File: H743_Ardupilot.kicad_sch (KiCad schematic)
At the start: 8 parts, among them U1 USBLC6-2P6

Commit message: upsadte SPI4 set to Baro
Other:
- sheet ANALOG_SENS ports: added ADC_AIRSPEED, ADC_VBAT1, ADC_VBAT2; removed none
- sheet MCU ports: added ADC_AIRSPEED, I2C1{I2C}, IMU1_CLKIN, IMU2_CLKIN, IMU2_DRDY, IMU3_A_CS, IMU3_G_CS, SPI3{SPI}; removed ADC_AIRS, ADC_VBAT1, ADC_VBAT2
- title: (none) -> H743_ARDUPILOT
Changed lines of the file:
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@@
 	(generator "eeschema")
 	(generator_version "10.0")
-	(paper "A4")
+	(paper "A3")
 	(title_block
+		(title "H743_ARDUPILOT")
 		(date "2026-09-24")
 	)
@@
 			)
 		)
-		(pin "ADC_AIRS" input
-			(at 120.65 82.55 180)
-			(effects
-				(font
-					(size 1.27 1.27)
-				)
-				(justify left)
-			)
-		)
 		(pin "ADC_CURR1" input
 			(at 170.18 101.6 0)
@@
 			)
 		)
-		(pin "ADC_VBAT1" input
-			(at 120.65 85.09 180)
-			(effects
-				(font
-					(size 1.27 1.27)
-				)
-				(justify left)
-			)
-		)
-		(pin "ADC_VBAT2" input
-			(at 120.65 87.63 180)
-			(effects
-				(font
-					(size 1.27 1.27)
-				)
-				(justify left)
-			)
-		)
 		(pin "LED_STRIP" input
 			(at 120.65 71.12 180)
@@
 		(pin "SPI2{SPI}" input
 			(at 170.18 90.17 0)
+			(effects
+				(font
+					(size 1.27 1.27)
+				)
+				(justify right)
+			)
+		)
+		(pin "ADC_AIRSPEED" input
+			(at 170.18 116.84 0)
+			(effects
+				(font
+					(size 1.27 1.27)
+				)
+				(justify right)
+			)
+		)
+		(pin "I2C1{I2C}" input
+			(at 170.18 106.68 0)
+			(effects
+				(font
+					(size 1.27 1.27)
+				)
+				(justify right)
+			)
+		)
+		(pin "IMU1_CLKIN" input
+			(at 170.18 109.22 0)
+			(effects
+				(font
+					(size 1.27 1.27)
+				)
+				(justify right)
+			)
+		)
+		(pin "IMU2_CLKIN" input
+			(at 170.18 111.76 0)
+			(effects
+				(font
+					(size 1.27 1.27)
+				)
+				(justify right)
+			)
+		)
+		(pin "IMU2_DRDY" output
+			(at 170.18 104.14 0)
+			(effects
+				(font
+					(size 1.27 1.27)
+				)
+				(justify right)
+			)
+		)
+		(pin "IMU3_A_CS" input
+			(at 170.18 135.89 0)
+			(effects
+				(font
+					(size 1.27 1.27)
+				)
+				(justify right)
+			)
+		)
+		(pin "IMU3_G_CS" input
+			(at 170.18 139.7 0)
+			(effects
+				(font
+					(size 1.27 1.27)
+				)
+				(justify right)
+			)
+		)
+		(pin "SPI3{SPI}" input
+			(at 170.18 148.59 0)
 			(effects
 				(font
@@
 			)
 		)
+		(pin "ADC_AIRSPEED" input
+			(at 182.88 116.84 180)
+			(effects
+				(font
+					(size 1.27 1.27)
+				)
+				(justify left)
+			)
+		)
+		(pin "ADC_VBAT1" input
+			(at 182.88 114.3 180)
+			(effects
+				(font
+					(size 1.27 1.27)
+				)
+				(justify left)
+			)
+		)
+		(pin "ADC_VBAT2" input
+			(at 182.88 119.38 180)
+			(effects
+				(font
+					(size 1.27 1.27)
+				)
+				(justify left)
+			)
+		)

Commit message: update 1
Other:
- sheet MCU ports: added ADC_VBAT1, ADC_VBAT2; removed none
- sheet POWER ports: added none; removed ADC_AIRS, ADC_VBAT1, ADC_VBAT2
- sheet SENSORS ports: added SPI2{SPI}; removed none
- moved on the sheet: H1, H2, H3, H4

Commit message: remove 9v_EN 9v power supply alwaye activated
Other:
- removed sheet POWER
- sheet MCU ports: added none; removed 9V_EN
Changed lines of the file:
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@@
-	(wire
-		(pts
-			(xy 101.6 90.17) (xy 120.65 90.17)
-		)
-		(stroke
-			(width 0)
-			(type default)
-		)
-	)
 	(wire
 		(pts
@@
 			)
 		)
-		(pin "9V_EN" input
-			(at 120.65 90.17 180)
-			(effects
-				(font
-					(size 1.27 1.27)
-				)
-				(justify left)
-			)
-		)
 		(pin "USB_OTG_P{USB}" input
 			(at 120.65 53.34 180)
@@
 				)
 			)
-		)
-	)
-	(sheet
-		(at 78.74 86.36)
-		(size 22.86 7.62)
-		(exclude_from_sim no)
-		(in_bom yes)
-		(on_board yes)
-		(dnp no)
-		(fields_autoplaced yes)
-		(stroke
-			(width 0.1524)
-			(type solid)
-		)
-		(fill
-			(color 0 0 0 0)
-		)
-		(property "Sheetname" "POWER"
-			(at 78.74 85.6484 0)
-			(show_name no)
-			(do_not_autoplace no)
-			(effects
-				(font
-					(size 1.27 1.27)
-				)
-				(justify left bottom)
-			)
-		)
-		(property "Sheetfile" "POWER.kicad_sch"
-			(at 78.74 94.5646 0)
-			(hide yes)
-			(show_name no)
-			(do_not_autoplace no)
-			(effects
-				(font
-					(size 1.27 1.27)
-				)
-				(justify left top)
-			)
-		)
-		(pin "9V_EN" input
-			(at 101.6 90.17 0)
-			(effects
-				(font
-					(size 1.27 1.27)
-				)
-				(justify right)
-			)
-		)
-		(instances
-			(project "H743_Ardupilot"
-				(path "/6b768b36-fce6-4be0-9021-6d41bddc3a70"
-					(page "3")
-				)
-			)

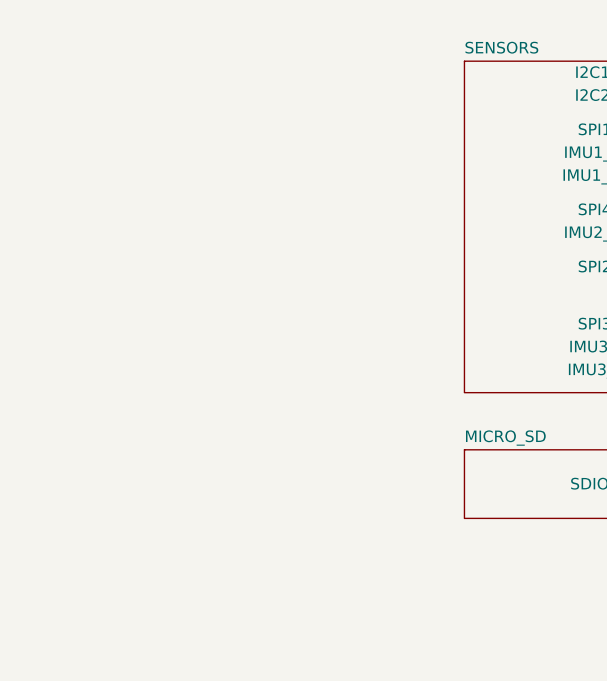
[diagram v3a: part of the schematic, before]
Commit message: add ANALOG_SENS sheet
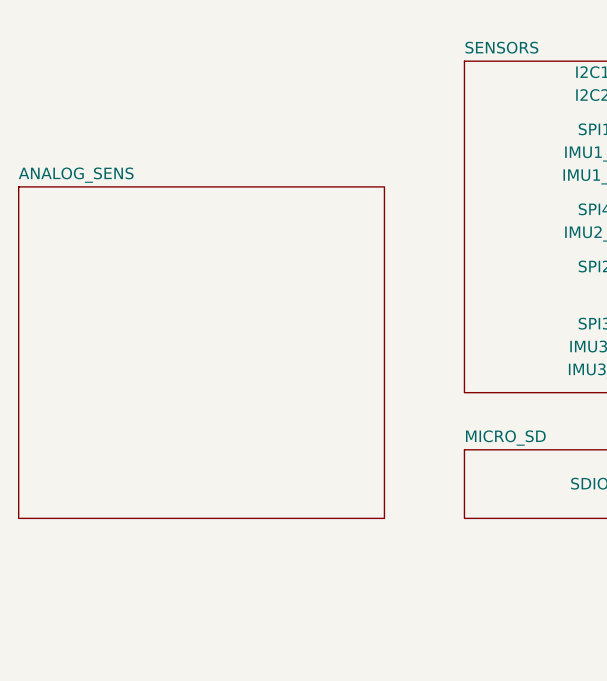
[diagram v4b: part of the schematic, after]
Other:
- sheet ANALOG_SENS: file untitled.kicad_sch -> ANALOG_SENS.kicad_sch
- sheet ANALOG_SENS ports: added none; removed ADC_AIRSPEED, ADC_VBAT1, ADC_VBAT2
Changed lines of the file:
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@@
+	)
+	(sheet
+		(at 29.21 113.03)
+		(size 40.64 36.83)
+		(exclude_from_sim no)
+		(in_bom yes)
+		(on_board yes)
+		(dnp no)
+		(fields_autoplaced yes)
+		(stroke
+			(width 0.1524)
+			(type solid)
+		)
+		(fill
+			(color 0 0 0 0)
+		)
+		(property "Sheetname" "ANALOG_SENS"
+			(at 29.21 112.3184 0)
+			(show_name no)
+			(do_not_autoplace no)
+			(effects
+				(font
+					(size 1.27 1.27)
+				)
+				(justify left bottom)
+			)
+		)
+		(property "Sheetfile" "ANALOG_SENS.kicad_sch"
+			(at 29.21 150.4446 0)
+			(hide yes)
+			(show_name no)
+			(do_not_autoplace no)
+			(effects
+				(font
+					(size 1.27 1.27)
+				)
+				(justify left top)
+			)
+		)
+		(instances
+			(project "H743_Ardupilot"
+				(path "/6b768b36-fce6-4be0-9021-6d41bddc3a70"
+					(page "3")
+				)
+			)
+		)
 	)
 	(sheet

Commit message: delete unused sheet
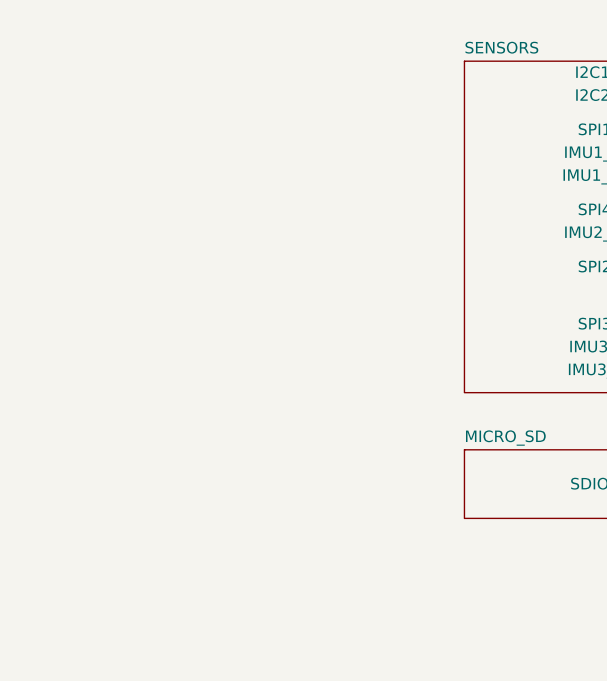
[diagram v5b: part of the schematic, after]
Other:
- sheet ANALOG_SENS ports: added ADC_AIRSPEED, ADC_VBAT1, ADC_VBAT2; removed none
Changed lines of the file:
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@@
 			)
 		)
-		(property "Sheetfile" "untitled.kicad_sch"
+		(property "Sheetfile" "ANALOG_SENS.kicad_sch"
 			(at 187.96 139.0146 0)
 			(hide yes)
@@
 				)
 			)
-		)
-	)
-	(sheet
-		(at 29.21 113.03)
-		(size 40.64 36.83)
-		(exclude_from_sim no)
-		(in_bom yes)
-		(on_board yes)
-		(dnp no)
-		(fields_autoplaced yes)
-		(stroke
-			(width 0.1524)
-			(type solid)
-		)
-		(fill
-			(color 0 0 0 0)
-		)
-		(property "Sheetname" "ANALOG_SENS"
-			(at 29.21 112.3184 0)
-			(show_name no)
-			(do_not_autoplace no)
-			(effects
-				(font
-					(size 1.27 1.27)
-				)
-				(justify left bottom)
-			)
-		)
-		(property "Sheetfile" "ANALOG_SENS.kicad_sch"
-			(at 29.21 150.4446 0)
-			(hide yes)
-			(show_name no)
-			(do_not_autoplace no)
-			(effects
-				(font
-					(size 1.27 1.27)
-				)
-				(justify left top)
-			)
-		)
-		(instances
-			(project "H743_Ardupilot"
-				(path "/6b768b36-fce6-4be0-9021-6d41bddc3a70"
-					(page "3")
-				)
-			)

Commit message: solved issue on SPI1
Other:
- added sheet POWER (POWER.kicad_sch)
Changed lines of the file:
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@@
+	)
+	(sheet
+		(at 38.1 114.3)
+		(size 36.83 27.94)
+		(exclude_from_sim no)
+		(in_bom yes)
+		(on_board yes)
+		(dnp no)
+		(fields_autoplaced yes)
+		(stroke
+			(width 0.1524)
+			(type solid)
+		)
+		(fill
+			(color 0 0 0 0)
+		)
+		(property "Sheetname" "POWER"
+			(at 38.1 113.5884 0)
+			(show_name no)
+			(do_not_autoplace no)
+			(effects
+				(font
+					(size 1.27 1.27)
+				)
+				(justify left bottom)
+			)
+		)
+		(property "Sheetfile" "POWER.kicad_sch"
+			(at 38.1 142.8246 0)
+			(show_name no)
+			(do_not_autoplace no)
+			(effects
+				(font
+					(size 1.27 1.27)
+				)
+				(justify left top)
+			)
+		)
+		(instances
+			(project "H743_Ardupilot"
+				(path "/6b768b36-fce6-4be0-9021-6d41bddc3a70"
+					(page "3")
+				)
+			)
+		)
 	)
 	(sheet

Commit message: fix MCU sensor hierarchy pin alignment
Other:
- sheet MCU ports: added IMU1_DRDY; removed IMU2_CLKIN
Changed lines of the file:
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@@
 			)
 		)
-		(pin "I2C2{I2C}" input
+		(pin "I2C2{I2C}" bidirectional
 			(at 120.65 81.28 180)
 			(effects
@@
 			)
 		)
-		(pin "SPI1{SPI}" input
+		(pin "SPI1{SPI}" bidirectional
 			(at 120.65 85.09 180)
 			(effects
@@
 			)
 		)
-		(pin "SPI4{SPI}" input
+		(pin "SPI4{SPI}" bidirectional
 			(at 120.65 93.98 180)
 			(effects
@@
 			)
 		)
-		(pin "SPI2{SPI}" input
+		(pin "SPI2{SPI}" bidirectional
 			(at 120.65 100.33 180)
 			(effects
@@
 			)
 		)
-		(pin "I2C1{I2C}" input
+		(pin "I2C1{I2C}" bidirectional
 			(at 120.65 78.74 180)
 			(effects
@@
 			)
 		)
-		(pin "IMU1_CLKIN" input
+		(pin "IMU1_DRDY" input
 			(at 120.65 87.63 180)
 			(effects
@@
 			)
 		)
-		(pin "IMU2_CLKIN" input
+		(pin "IMU1_CLKIN" output
 			(at 120.65 90.17 180)
 			(effects
@@
 			)
 		)
-		(pin "IMU2_DRDY" output
+		(pin "IMU2_DRDY" input
 			(at 120.65 96.52 180)
 			(effects
@@
 			)
 		)
-		(pin "IMU3_A_CS" input
+		(pin "IMU3_A_CS" output
 			(at 120.65 109.22 180)
 			(effects
@@
 			)
 		)
-		(pin "IMU3_G_CS" input
+		(pin "IMU3_G_CS" output
 			(at 120.65 111.76 180)
 			(effects
@@
 			)
 		)
-		(pin "SPI3{SPI}" input
+		(pin "SPI3{SPI}" bidirectional
 			(at 120.65 106.68 180)
 			(effects
